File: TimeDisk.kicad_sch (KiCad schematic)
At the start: 65 parts, among them J1 AppleIIBus, J2 microUSB, SW1 Mode, U1 EPM7128SL84, U2 DS1315S-5, U3 74AHCT04, U4 AS6C8008, U5 39F040, U6 XC6206P332MR, U7 CH340G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

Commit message: Add timer
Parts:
- removed R1, R3: 15, stdpads:R_0805, symbol Device:R_Small
- added C29: 10u, stdpads:C_0805, symbol Device:C_Small
- added C30: 2u2, stdpads:C_0805, symbol Device:C_Small
- added R15: 4k7, stdpads:R_0805, symbol Device:R_Small
- added R16: 15, stdpads:R_0805, symbol Device:R_Small
- added R17, R19, R21: DNP, stdpads:R_0805, symbol Device:R_Small
- added R18, R20: 22k, stdpads:R_0805, symbol Device:R_Small
- added U8: 74LVC1G74DC, stdpads:NXP_VSSOP-8_2.3x2mm, symbol GW_Logic:741G74DC
- added U9: 74AHCT1G125GW, stdpads:SOT-353, symbol GW_Logic:741G125GW
- R10, R11, R13: value 10k -> 22k
- R9: value 100 -> 15
- U3: value 74AHCT04 -> 74LVC04AD
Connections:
- net 7Mr is gone; now on net 7M: U1.83 (GClk1)
- net PHI1r is gone; now on net PHI1: U1.2 (OE2/GClk2)
- net +3V3: now also C29.1, U8.6 (~{R}), U8.7 (~{S}), U8.8 (Vcc)
- net +5V: now also C30.1, R18.1, R20.1, U9.5 (Vcc); no longer U7.10 (~{DSR}), U7.11 (~{RI})
- net GND: now also C29.2, C30.2, R15.1, R17.2, R19.2, R21.2, U8.4 (GND), U9.2 (A), U9.3 (GND)
- net RA0: now also U8.2 (D)
- net RA1: now also U8.1 (CK)
- net RA2: now also R15.2
- net ~{IRQ}: now also U9.4 (Y)
- net ID2: now reaches R13.2, U7.12 (~{DCD})
- net ID2: now also R17.1
- new net: R16.2, U8.5 (Q)
- new net ID0: R20.2, R21.1, U7.10 (~{DSR})
- new net ID1: R18.2, R19.1, U7.11 (~{RI})
- new net IRQ~{OE}: R16.1, U9.1 (~{OE})
- no-connect marks 4 -> 5
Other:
- moved on the sheet: C11, C13, C23, C24, C8, J2, R10, R11, R12, R13, R7, R8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

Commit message: idk if it's even good
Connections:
- net CH340G3V3 is gone; now on net +3V3: C25.1, U7.4 (V3)
- net +3V3: now also C27.1, U7.16 (VCC)
- net +5V: no longer C27.1, U7.16 (VCC)
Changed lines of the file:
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@@
   (junction (at 128.27 179.07) (diameter 0) (color 0 0 0 0)
   )
+  (junction (at 170.18 160.02) (diameter 0) (color 0 0 0 0)
+  )
   (junction (at 15.24 140.97) (diameter 0) (color 0 0 0 0)
   )
@@
   (junction (at 99.06 129.54) (diameter 0) (color 0 0 0 0)
   )
+  (junction (at 215.9 25.4) (diameter 0) (color 0 0 0 0)
+  )
   (junction (at 93.98 129.54) (diameter 0) (color 0 0 0 0)
   )
@@
     (stroke (width 0) (type default))
   )
+  (wire (pts (xy 215.9 25.4) (xy 218.44 25.4))
+    (stroke (width 0) (type default))
+  )
   (wire (pts (xy 134.62 121.92) (xy 127 121.92))
     (stroke (width 0) (type default))
@@
     (stroke (width 0) (type default))
   )
+  (wire (pts (xy 170.18 160.02) (xy 185.42 160.02))
+    (stroke (width 0) (type default))
+  )
   (wire (pts (xy 109.22 78.74) (xy 119.38 78.74))
     (stroke (width 0) (type default))
@@
     (stroke (width 0) (type default))
   )
-  (wire (pts (xy 170.18 158.75) (xy 170.18 160.02))
-    (stroke (width 0) (type default))
-  )
   (wire (pts (xy 226.06 40.64) (xy 246.38 40.64))
     (stroke (width 0) (type default))
@@
     (effects (font (size 1.27 1.27)) (justify right bottom))
   )
-  (global_label "CH340G3V3" (shape input) (at 218.44 25.4 0) (fields_autoplaced)
-    (effects (font (size 1.27 1.27)) (justify left))
-    (property "Intersheetrefs" "${INTERSHEET_REFS}" (at 231.7709 25.3206 0)
-      (effects (font (size 1.27 1.27)) (justify left) hide)
-    )
-  )
-  (global_label "CH340G3V3" (shape input) (at 170.18 158.75 0) (fields_autoplaced)
-    (effects (font (size 1.27 1.27)) (justify left))
-    (property "Intersheetrefs" "${INTERSHEET_REFS}" (at 183.5109 158.6706 0)
-      (effects (font (size 1.27 1.27)) (justify left) hide)
-    )
-  )
   (symbol (lib_id "GW_PLD:EPM7128SL84") (at 90.17 76.2 0) (unit 1)
     (in_bom yes) (on_board yes) (dnp no)
@@
     )
   )
+  (symbol (lib_id "power:+3V3") (at 170.18 160.02 0) (unit 1)
+    (in_bom yes) (on_board yes) (dnp no)
+    (property "Reference" "#PWR02" (at 170.18 163.83 0)
+      (effects (font (size 1.27 1.27)) hide)
+    )
+    (property "Value" "+3V3" (at 170.18 156.21 0)
+      (effects (font (size 1.27 1.27)))
+    )
+    (property "Footprint" "" (at 170.18 160.02 0)
+      (effects (font (size 1.27 1.27)) hide)
+    )
+    (property "Datasheet" "" (at 170.18 160.02 0)
+      (effects (font (size 1.27 1.27)) hide)
+    )
+    (pin "1")
+    (instances
+      (project "TimeDisk"
+        (path "/4fa10683-33cd-4dcd-8acc-2415cd63c62a"
+          (reference "#PWR02") (unit 1)
+        )
+      )
+    )
+  )
   (symbol (lib_id "power:GND") (at 245.11 88.9 0) (mirror y) (unit 1)
     (in_bom yes) (on_board yes) (dnp no)
@@
     )
   )
-  (symbol (lib_id "power:+5V") (at 215.9 25.4 0) (unit 1)
+  (symbol (lib_id "power:+3V3") (at 215.9 25.4 0) (unit 1)
     (in_bom yes) (on_board yes) (dnp no)
-    (property "Reference" "#PWR02" (at 215.9 29.21 0)
+    (property "Reference" "#PWR06" (at 215.9 29.21 0)
       (effects (font (size 1.27 1.27)) hide)
     )
-    (property "Value" "+5V" (at 215.9 21.59 0)
+    (property "Value" "+3V3" (at 215.9 21.59 0)
       (effects (font (size 1.27 1.27)))
     )
@@
       (project "TimeDisk"
         (path "/4fa10683-33cd-4dcd-8acc-2415cd63c62a"
-          (reference "#PWR02") (unit 1)
+          (reference "#PWR06") (unit 1)
         )
       )
@@
         )
       )
-    )
-  )
-  (symbol (lib_id "power:+5V") (at 185.42 160.02 0) (unit 1)
-    (in_bom yes) (on_board yes) (dnp no)
-    (property "Reference" "#PWR06" (at 185.42 163.83 0)
-      (effects (font (size 1.27 1.27)) hide)
-    )
-    (property "Value" "+5V" (at 185.42 156.21 0)
-      (effects (font (size 1.27 1.27)))
-    )
-    (property "Footprint" "" (at 185.42 160.02 0)
-      (effects (font (size 1.27 1.27)) hide)
-    )
-    (property "Datasheet" "" (at 185.42 160.02 0)
-      (effects (font (size 1.27 1.27)) hide)
-    )
-    (pin "1")
-    (instances
-      (project "TimeDisk"
-        (path "/4fa10683-33cd-4dcd-8acc-2415cd63c62a"
-          (reference "#PWR06") (unit 1)
-        )
-      )

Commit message: Done?
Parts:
- removed R11, R13, R18, R20: 22k, stdpads:R_0805, symbol Device:R_Small
- removed R17, R19, R21: DNP, stdpads:R_0805, symbol Device:R_Small
- added R1: DNP, stdpads:R_0805, symbol Device:R_Small
- added R3: 1k, stdpads:R_0805, symbol Device:R_Small
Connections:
- net ID0 is gone; now on net +5V: U7.10 (~{DSR})
- net ID1 is gone; now on net +5V: U7.11 (~{RI})
- net +3V3: no longer C25.1, C27.1, U7.16 (VCC), U7.4 (V3)
- net +5V: now also C27.1, U7.16 (VCC), R1.1
- net GND: now also U7.15 (R232), R3.2
- net ID2 renamed ~{DCD}
- net ~{DCD}: now also R1.2, R3.1
- new net CH340_3V3: C25.1, U7.4 (V3)

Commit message: As sent to JLC
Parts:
- added J3: JTAG, stdpads:Header_2x5_Unshrouded_P1.27mm, symbol Connector_Generic:Conn_02x05_Odd_Even
- added R11, R13: 22k, stdpads:R_0805, symbol Device:R_Small
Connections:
- net +5V: now also J3.4 (Pin_4), R13.1
- net GND: now also J3.10 (Pin_10), J3.2 (Pin_2), R11.2
- net TCK: now also R11.1
- net TDI: now also J3.9 (Pin_9)
- net TDO: now also J3.3 (Pin_3)
- net TMS: now also J3.5 (Pin_5), R13.2
- net TCKr: now reaches R12.1, U7.2 (TXD)
- net TCKr: now also J3.1 (Pin_1)
- no-connect marks 5 -> 8
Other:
- moved on the sheet: R12

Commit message: Add RPP
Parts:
- added D1, D2: 1N5819, stdpads:D_SOD-123, symbol Device:D_Schottky_Small_Filled
- added D3: 10V, stdpads:D_SOD-323, symbol Device:D_Zener_Small_Filled
- added Q1: AO3401A, stdpads:SOT-23, symbol Transistor_FET:AO3401A
- added R14, R17: 220, stdpads:R_0805, symbol Device:R_Small
- BT1: LCSC Part (none) -> C964833
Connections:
- net +BATT: now also D1.1 (K), D2.1 (K), D3.1 (K), Q1.2 (S); no longer BT1.1 (+)
- net GND: now also D2.2 (A), R14.1; no longer U3.7 (GND)
- new net: BT1.1 (+), R17.2
- new net: D3.2 (A), Q1.1 (G), R14.2
- new net: D1.2 (A), Q1.3 (D), R17.1
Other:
- moved on the sheet: C23, C24, J2, R1, R10, R12, R3, U7, Y2

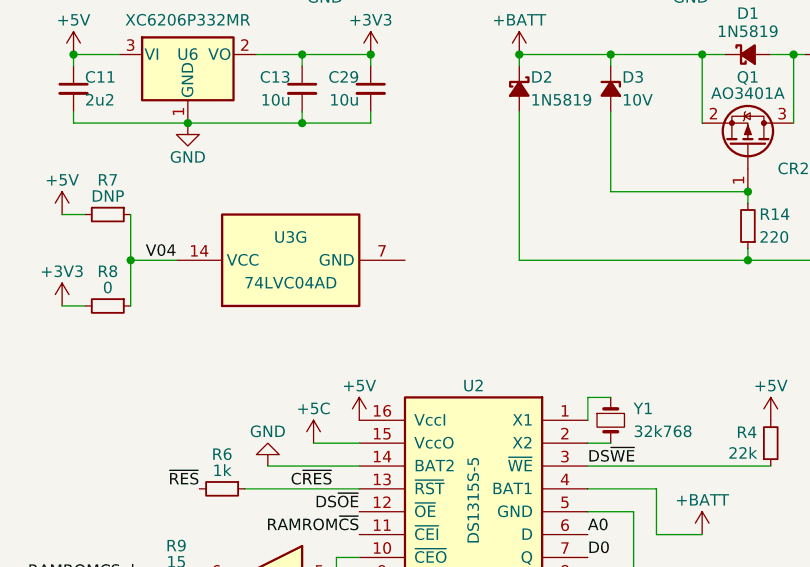
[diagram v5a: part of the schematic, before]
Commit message: Update via-to-via clearance rules and update footprints
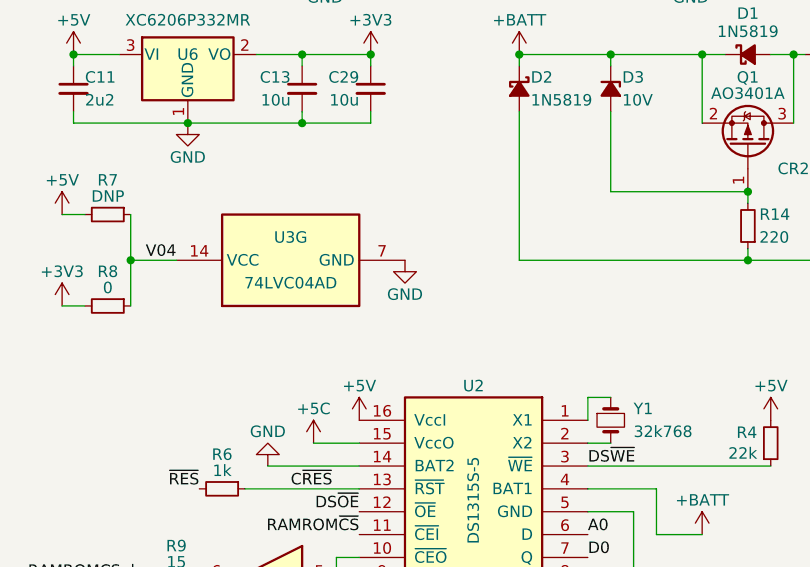
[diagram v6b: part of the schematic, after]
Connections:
- net GND: now also U3.7 (GND)
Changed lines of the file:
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@@
+    )
+  )
+  (symbol (lib_id "power:GND") (at 209.55 88.9 0) (mirror y) (unit 1)
+    (in_bom yes) (on_board yes) (dnp no)
+    (property "Reference" "#PWR027" (at 209.55 95.25 0)
+      (effects (font (size 1.27 1.27)) hide)
+    )
+    (property "Value" "GND" (at 209.55 92.71 0)
+      (effects (font (size 1.27 1.27)))
+    )
+    (property "Footprint" "" (at 209.55 88.9 0)
+      (effects (font (size 1.27 1.27)) hide)
+    )
+    (property "Datasheet" "" (at 209.55 88.9 0)
+      (effects (font (size 1.27 1.27)) hide)
+    )
+    (pin "1")
+    (instances
+      (project "TimeDisk"
+        (path "/4fa10683-33cd-4dcd-8acc-2415cd63c62a"
+          (reference "#PWR027") (unit 1)
+        )
+      )
     )
   )

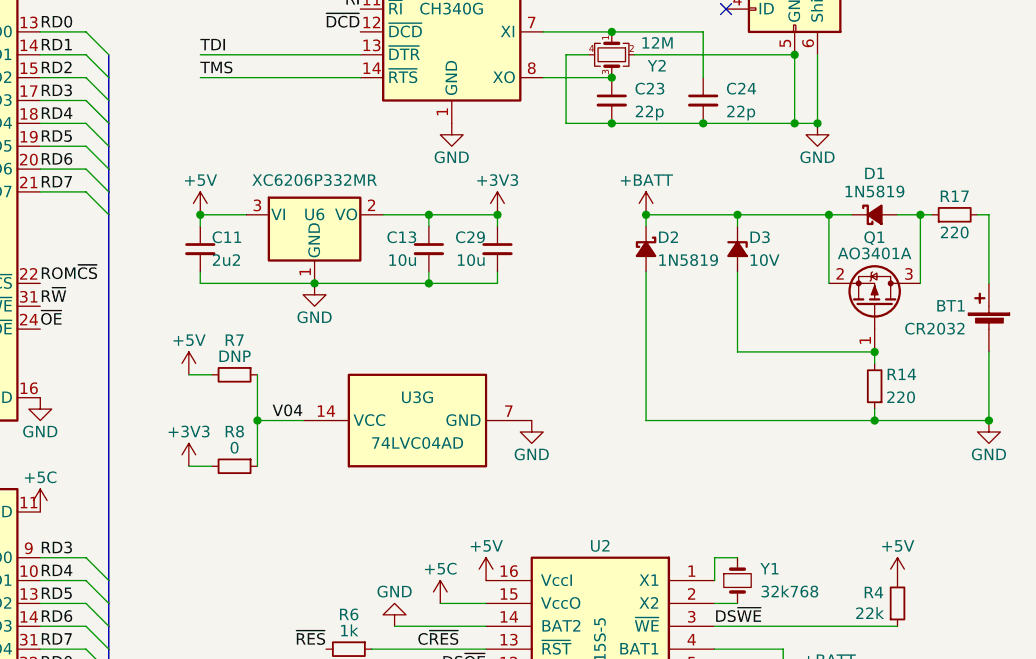
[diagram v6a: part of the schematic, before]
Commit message: with hole
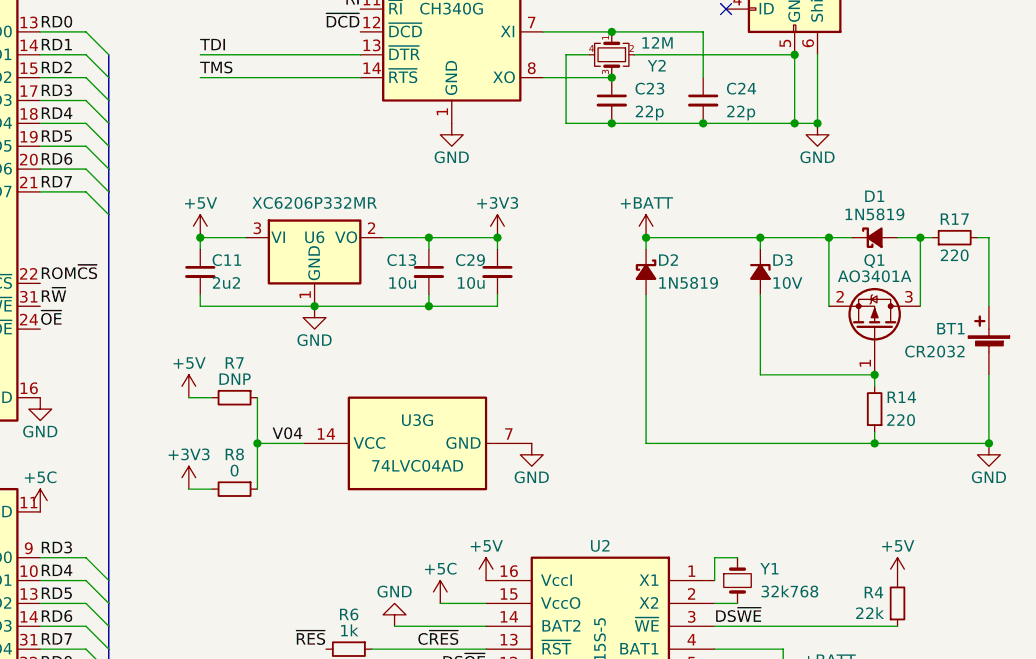
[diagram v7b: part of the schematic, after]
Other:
- title: Time Machine -> GW4206B (TimeDisk)
- moved on the sheet: BT1, C11, C13, C29, D1, D2, D3, Q1, R14, R17, R7, R8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

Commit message: RC 1.1
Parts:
- removed R1: DNP, stdpads:R_0805, symbol Device:R_Small
- removed R15: 4k7, stdpads:R_0805, symbol Device:R_Small
- removed R3: 1k, stdpads:R_0805, symbol Device:R_Small
- D3: value 10V -> 6V8
- R11, R13: value 22k -> DNP; LCSC Part C17560 -> (none); Mfg. Part Numbers Uniroyal 0805W8F2202T5E -> (none); Notes Any manufacturer's part is acceptable. -> (none)
- U8: footprint stdpads:NXP_VSSOP-8_2.3x2mm -> stdpads:NXP_TSSOP-8_3x3mm_P0.65mm
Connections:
- net ~{DCD} is gone; now on net +5V: U7.12 (~{DCD})
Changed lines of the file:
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@@
   (junction (at 97.79 191.77) (diameter 0) (color 0 0 0 0)
   )
-  (junction (at 248.92 22.86) (diameter 0) (color 0 0 0 0)
-  )
   (junction (at 205.74 68.58) (diameter 0) (color 0 0 0 0)
   )
@@
     (stroke (width 0) (type default))
   )
-  (wire (pts (xy 24.13 190.5) (xy 29.21 190.5))
-    (stroke (width 0) (type default))
-  )
   (wire (pts (xy 86.36 25.4) (xy 88.9 25.4))
     (stroke (width 0) (type default))
@@
     (stroke (width 0) (type default))
   )
+  (wire (pts (xy 248.92 17.78) (xy 248.92 22.86))
+    (stroke (width 0) (type default))
+  )
   (bus (pts (xy 124.46 73.66) (xy 124.46 76.2))
     (stroke (width 0) (type default))
@@
     (effects (font (size 1.27 1.27)) (justify right bottom))
   )
-  (label "RA2" (at 24.13 190.5 0) (fields_autoplaced)
-    (effects (font (size 1.27 1.27)) (justify left bottom))
-  )
   (label "A12" (at 109.22 55.88 0) (fields_autoplaced)
     (effects (font (size 1.27 1.27)) (justify left bottom))
@@
       (effects (font (size 1.27 1.27)) (justify right))
     )
-    (property "Value" "22k" (at 40.64 156.21 0)
+    (property "Value" "DNP" (at 40.64 156.21 0)
       (effects (font (size 1.27 1.27)) (justify right))
     )
@@
       (effects (font (size 1.27 1.27)) hide)
     )
-    (property "LCSC Part" "C17560" (at 39.37 154.94 0)
-      (effects (font (size 1.27 1.27)) hide)
-    )
-    (property "Mfg. Part Numbers" "Uniroyal 0805W8F2202T5E" (at 39.37 154.94 0)
-      (effects (font (size 1.27 1.27)) hide)
-    )
-    (property "Notes" "Any manufacturer's part is acceptable." (at 39.37 154.94 0)
+    (property "Notes" "" (at 39.37 154.94 0)
       (effects (font (size 1.27 1.27)) hide)
     )
@@
     )
   )
-  (symbol (lib_id "power:GND") (at 248.92 27.94 0) (mirror y) (unit 1)
-    (in_bom yes) (on_board yes) (dnp no)
-    (property "Reference" "#PWR018" (at 248.92 34.29 0)
-      (effects (font (size 1.27 1.27)) hide)
-    )
-    (property "Value" "GND" (at 248.92 31.75 0)
-      (effects (font (size 1.27 1.27)))
-    )
-    (property "Footprint" "" (at 248.92 27.94 0)
-      (effects (font (size 1.27 1.27)) hide)
-    )
-    (property "Datasheet" "" (at 248.92 27.94 0)
-      (effects (font (size 1.27 1.27)) hide)
-    )
-    (pin "1")
-    (instances
-      (project "TimeDisk"
-        (path "/4fa10683-33cd-4dcd-8acc-2415cd63c62a"
-          (reference "#PWR018") (unit 1)
-        )
-      )
-    )
-  )
   (symbol (lib_id "Regulator_Linear:XC6206PxxxMR") (at 185.42 68.58 0) (unit 1)
     (in_bom yes) (on_board yes) (dnp no)
@@
     )
   )
-  (symbol (lib_id "power:GND") (at 29.21 195.58 0) (unit 1)
-    (in_bom yes) (on_board yes) (dnp no)
-    (property "Reference" "#PWR017" (at 29.21 201.93 0)
-      (effects (font (size 1.27 1.27)) hide)
-    )
-    (property "Value" "GND" (at 29.21 199.39 0)
-      (effects (font (size 1.27 1.27)))
-    )
-    (property "Footprint" "" (at 29.21 195.58 0)
-      (effects (font (size 1.27 1.27)) hide)
-    )
-    (property "Datasheet" "" (at 29.21 195.58 0)
-      (effects (font (size 1.27 1.27)) hide)
-    )
-    (pin "1")
-    (instances
-      (project "TimeDisk"
-        (path "/4fa10683-33cd-4dcd-8acc-2415cd63c62a"
-          (reference "#PWR017") (unit 1)
-        )
-      )
-    )
-  )
   (symbol (lib_id "Device:R_Small") (at 247.65 87.63 180) (unit 1)
     (in_bom yes) (on_board yes) (dnp no)
@@
     )
   )
-  (symbol (lib_id "Device:R_Small") (at 248.92 25.4 0) (mirror y) (unit 1)
-    (in_bom yes) (on_board yes) (dnp no)
-    (property "Reference" "R3" (at 250.19 24.13 0)
-      (effects (font (size 1.27 1.27)) (justify right))
-    )
-    (property "Value" "1k" (at 250.19 26.67 0)
-      (effects (font (size 1.27 1.27)) (justify right))
-    )
-    (property "Footprint" "stdpads:R_0805" (at 248.92 25.4 0)
-      (effects (font (size 1.27 1.27)) hide)
-    )
-    (property "Datasheet" "~" (at 248.92 25.4 0)
-      (effects (font (size 1.27 1.27)) hide)
-    )
-    (property "LCSC Part" "" (at 248.92 25.4 0)
-      (effects (font (size 1.27 1.27)) hide)
-    )
-    (pin "1")
-    (pin "2")
-    (instances
-      (project "TimeDisk"
-        (path "/4fa10683-33cd-4dcd-8acc-2415cd63c62a"
-          (reference "R3") (unit 1)
-        )
-      )
-    )
-  )
   (symbol (lib_id "Device:C_Small") (at 97.79 168.91 0) (unit 1)
     (in_bom yes) (on_board yes) (dnp no)
@@
       (effects (font (size 1.27 1.27)))
     )
-    (property "Footprint" "stdpads:NXP_VSSOP-8_2.3x2mm" (at 144.78 35.56 0)
+    (property "Footprint" "stdpads:NXP_TSSOP-8_3x3mm_P0.65mm" (at 144.78 35.56 0)
       (effects (font (size 1.27 1.27)) (justify top) hide)
     )
@@
     )
   )
-  (symbol (lib_id "Device:R_Small") (at 29.21 193.04 0) (mirror x) (unit 1)
-    (in_bom yes) (on_board yes) (dnp no)
-    (property "Reference" "R15" (at 27.94 191.77 0)
-      (effects (font (size 1.27 1.27)) (justify right))
-    )
-    (property "Value" "4k7" (at 27.94 194.31 0)
-      (effects (font (size 1.27 1.27)) (justify right))
-    )
-    (property "Footprint" "stdpads:R_0805" (at 29.21 193.04 0)
-      (effects (font (size 1.27 1.27)) hide)
-    )
-    (property "Datasheet" "~" (at 29.21 193.04 0)
-      (effects (font (size 1.27 1.27)) hide)
-    )
-    (pin "1")
-    (pin "2")
-    (instances
-      (project "TimeDisk"
-        (path "/4fa10683-33cd-4dcd-8acc-2415cd63c62a"
-          (reference "R15") (unit 1)
-        )
-      )
-    )
-  )
   (symbol (lib_id "Device:C_Small") (at 172.72 72.39 0) (unit 1)
     (in_bom yes) (on_board yes) (dnp no)
@@
       (effects (font (size 1.27 1.27)) (justify right))
     )
-    (property "Value" "22k" (at 50.8 156.21 0)
+    (property "Value" "DNP" (at 50.8 156.21 0)
       (effects (font (size 1.27 1.27)) (justify right))
     )
@@
       (effects (font (size 1.27 1.27)) hide)
     )
-    (property "LCSC Part" "C17560" (at 49.53 154.94 0)
-      (effects (font (size 1.27 1.27)) hide)
-    )
-    (property "Mfg. Part Numbers" "Uniroyal 0805W8F2202T5E" (at 49.53 154.94 0)
-      (effects (font (size 1.27 1.27)) hide)
-    )
-    (property "Notes" "Any manufacturer's part is acceptable." (at 49.53 154.94 0)
+    (property "Notes" "" (at 49.53 154.94 0)
       (effects (font (size 1.27 1.27)) hide)
     )
@@
     )
   )
-  (symbol (lib_id "Device:R_Small") (at 248.92 20.32 0) (mirror y) (unit 1)
-    (in_bom yes) (on_board yes) (dnp no)
-    (property "Reference" "R1" (at 250.19 19.05 0)
-      (effects (font (size 1.27 1.27)) (justify right))
-    )
-    (property "Value" "DNP" (at 250.19 21.59 0)
-      (effects (font (size 1.27 1.27)) (justify right))
-    )
-    (property "Footprint" "stdpads:R_0805" (at 248.92 20.32 0)
-      (effects (font (size 1.27 1.27)) hide)
-    )
-    (property "Datasheet" "~" (at 248.92 20.32 0)
-      (effects (font (size 1.27 1.27)) hide)
-    )
-    (pin "1")
-    (pin "2")
-    (instances
-      (project "TimeDisk"
-        (path "/4fa10683-33cd-4dcd-8acc-2415cd63c62a"
-          (reference "R1") (unit 1)
-        )
-      )
-    )
-  )
   (symbol (lib_id "Device:C_Small") (at 185.42 162.56 0) (unit 1)
     (in_bom yes) (on_board yes) (dnp no)
@@
       (effects (font (size 1.27 1.27)) (justify left))
     )
-    (property "Value" "10V" (at 236.22 73.66 90)
+    (property "Value" "6V8" (at 236.22 73.66 90)
       (effects (font (size 1.27 1.27)) (justify left))
     )
